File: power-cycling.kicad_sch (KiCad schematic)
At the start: 0 parts

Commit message: Updated sch power cycling section
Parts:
- added C?: C_100n_0402, antmicro-footprints:C_0402_1005Metric, symbol antmicroCapacitors0402:C_100n_0402
- added D? (x8): BZT52B15SV-T, antmicro-footprints:SOD-323, symbol antmicroDiodesZenerSingle:BZT52B15SV-T
- added Q? (x8): 2N7002K-T1-E3, antmicro-footprints:SOT-23-3, symbol antmicroTransistorsFETsMOSFETsSingle:2N7002K-T1-E3
- added QA? (x8), QB? (x8): SI7613DN-T1-GE3, antmicro-footprints:Vishay_PowerPAK_1212-8_Single, symbol antmicroTransistorsFETsMOSFETsSingle:SI7613DN-T1-GE3
- added R? (x6): R_0R_0402, antmicro-footprints:R_0402_1005Metric, symbol antmicroResistors0402:R_0R_0402
- added R? (x16): R_10k_0402, antmicro-footprints:R_0402_1005Metric, symbol antmicroResistors0402:R_10k_0402
- added R? (x16): R_2R_0402, antmicro-footprints:0402-res, symbol antmicroResistors0402:R_2R_0402
- added R? (x9): R_4k7_0402, antmicro-footprints:R_0402_1005Metric, symbol antmicroResistors0402:R_4k7_0402
- added TP? (x8): TP_1mm_SMD, antmicro-footprints:TP_SMD_1mm, symbol antmicroTestPoints:TP_1mm_SMD
- added U?: TCA9534, gpu-cluster-backplane-footprints:TSSOP-16, symbol gpu-cluster-backplane:TCA9534
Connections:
- new net: R?.1, R?.2, U?.3 (A2)
- new net: R?.1, R?.2, U?.1 (A0)
- new net: R?.2, U?.13 (~{INT})
- new net: R?.1, R?.2, U?.2 (A1)
- new net: QA?.4 (G), R?.2 (x8)
- new net: D?.A, Q?.3 (D), R?.1, R?.1, R?.2 (x8)
- new net: QB?.4 (G), R?.2 (x8)
- new net C_MEAS_1: QA?.5 (D), QB?.5 (D)
- new net C_MEAS_2: QA?.5 (D), QB?.5 (D)
- new net C_MEAS_3: QA?.5 (D), QB?.5 (D)
- new net C_MEAS_4: QA?.5 (D), QB?.5 (D)
- new net C_MEAS_5: QA?.5 (D), QB?.5 (D)
- new net C_MEAS_6: QA?.5 (D), QB?.5 (D)
- new net C_MEAS_7: QA?.5 (D), QB?.5 (D)
- new net C_MEAS_8: QA?.5 (D), QB?.5 (D)
- new net GND: C?.2, Q?.2 (S), Q?.2 (S), Q?.2 (S), Q?.2 (S), Q?.2 (S), Q?.2 (S), Q?.2 (S), Q?.2 (S), R?.2, R?.2, R?.2, R?.2, R?.2, R?.2, R?.2, R?.2, R?.2, R?.2, R?.2, U?.8 (GND)
- new net PC_1: Q?.1 (G), R?.1, R?.2, TP?.1, U?.4 (P0)
- new net PC_2: Q?.1 (G), R?.1, R?.2, TP?.1, U?.5 (P1)
- new net PC_3: Q?.1 (G), R?.1, R?.2, TP?.1, U?.6 (P2)
- new net PC_4: Q?.1 (G), R?.1, R?.2, TP?.1, U?.7 (P3)
- new net PC_5: Q?.1 (G), R?.1, R?.2, TP?.1, U?.9 (P4)
- new net PC_6: Q?.1 (G), R?.1, R?.2, TP?.1, U?.10 (P5)
- new net PC_7: Q?.1 (G), R?.1, R?.2, TP?.1, U?.11 (P6)
- new net PC_8: Q?.1 (G), R?.1, R?.2, TP?.1, U?.12 (P7)
- new net SCL: U?.14 (SCL)
- new net SDA: U?.15 (SDA)
- new net VCC12V0: D?.K, D?.K, D?.K, D?.K, D?.K, D?.K, D?.K, D?.K, QA?.1 (S), QA?.1 (S), QA?.1 (S), QA?.1 (S), QA?.1 (S), QA?.1 (S), QA?.1 (S), QA?.1 (S), QA?.2 (S), QA?.2 (S), QA?.2 (S), QA?.2 (S), QA?.2 (S), QA?.2 (S), QA?.2 (S), QA?.2 (S), QA?.3 (S), QA?.3 (S), QA?.3 (S), QA?.3 (S), QA?.3 (S), QA?.3 (S), QA?.3 (S), QA?.3 (S), QB?.1 (S), QB?.1 (S), QB?.1 (S), QB?.1 (S), QB?.1 (S), QB?.1 (S), QB?.1 (S), QB?.1 (S), QB?.2 (S), QB?.2 (S), QB?.2 (S), QB?.2 (S), QB?.2 (S), QB?.2 (S), QB?.2 (S), QB?.2 (S), QB?.3 (S), QB?.3 (S), QB?.3 (S), QB?.3 (S), QB?.3 (S), QB?.3 (S), QB?.3 (S), QB?.3 (S), R?.1, R?.1, R?.1, R?.1, R?.1, R?.1, R?.1, R?.1
- new net VCC3V3: C?.1, R?.1, R?.1, R?.1, R?.1, R?.1, R?.1, R?.1, R?.1, R?.1, R?.1, R?.1, R?.1, U?.16 (VDD)
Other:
- note added: "Arbiter for powering channels"
- note added: "GPIO EXPANDER for power cycling"
- note added: "I2C adress: 0x20"
- note added: "Key transistors' polarization TPs"
- note added: "Power Cycling"
- note added: "Power switching transistors"
- note added: "Remarks: Power can be switched on when: - signals from GPIO expander is enabled (pulled low) - GPU card module is inserted into slot"
- note added: "UP TO 15A"

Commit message: WIP Standarization
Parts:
- removed R? (x6): R_0R_0402, antmicro-footprints:R_0402_1005Metric, symbol antmicroResistors0402:R_0R_0402
- removed R?: R_4k7_0402, antmicro-footprints:R_0402_1005Metric, symbol antmicroResistors0402:R_4k7_0402
- removed U?: TCA9534, gpu-cluster-backplane-footprints:TSSOP-16, symbol gpu-cluster-backplane:TCA9534
- added R? (x6): R_0R_0402, antmicro-footprints:R_0402_1005Metric, symbol antmicroResistors0402:R_0R_0402
- added R?: R_4k7_0402, antmicro-footprints:R_0402_1005Metric, symbol antmicroResistors0402:R_4k7_0402
- added U?: TCA9534PWR, antmicro-footprints:TSSOP-16_4.4x5mm_P0.65mm, symbol antmicroInterfaceIOExpanders:TCA9534PWR
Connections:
- net GND: now also R?.2, R?.2, R?.2, U?.8 (GND)
- net PC_1: now also U?.4 (P0)
- net PC_2: now also U?.5 (P1)
- net PC_3: now also U?.6 (P2)
- net PC_4: now also U?.7 (P3)
- net PC_5: now also U?.9 (P4)
- net PC_6: now also U?.10 (P5)
- net PC_7: now also U?.11 (P6)
- net PC_8: now also U?.12 (P7)
- net SCL: now also U?.14 (SCL)
- net SDA: now also U?.15 (SDA)
- net VCC3V3: now also R?.1, R?.1, R?.1, R?.1, U?.16 (VDD)
- new net: R?.1, R?.2, U?.1 (A0)
- new net: R?.2, U?.13 (~{INT})
- new net: R?.1, R?.2, U?.2 (A1)
- new net: R?.1, R?.2, U?.3 (A2)
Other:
- moved on the sheet: C?

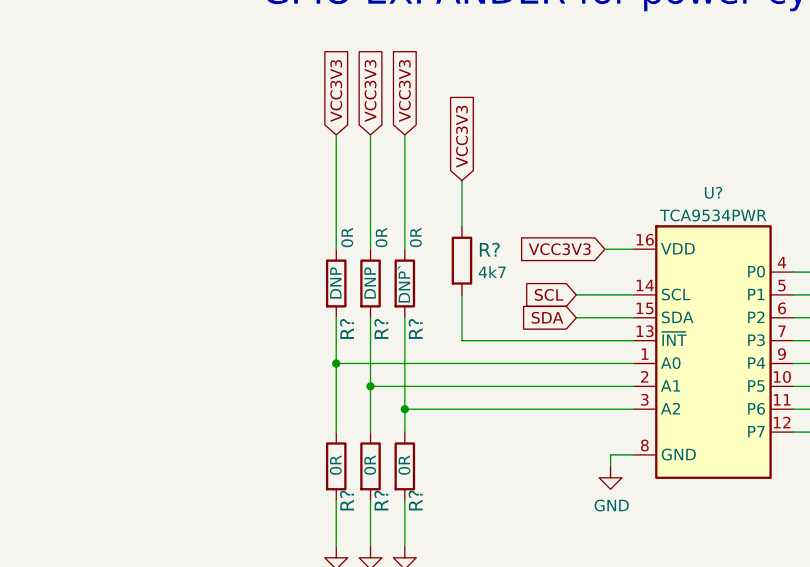
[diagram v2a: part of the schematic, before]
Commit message: Added debug section to schematic
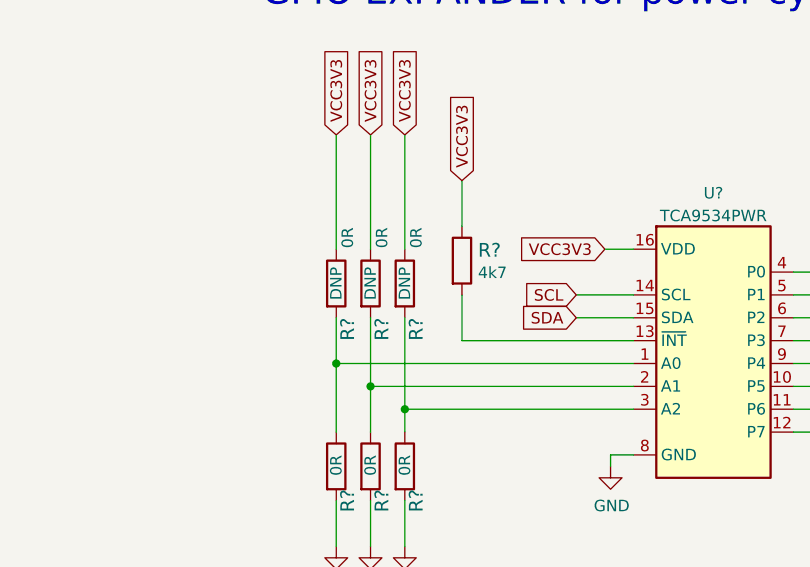
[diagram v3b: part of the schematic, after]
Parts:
- R?: DNP DNP` -> DNP
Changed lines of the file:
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@@
     )
     (property "Val" "0R" (id 6) (at 333.375 184.785 0))
-    (property "DNP" "DNP`" (id 7) (at 332.105 189.865 0))
+    (property "DNP" "DNP" (id 7) (at 332.105 189.865 0))
     (pin "1")
     (pin "2")

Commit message: Added function for enabling power after insertion of the card
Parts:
- added R? (x16): R_0R_0402, antmicro-footprints:R_0402_1005Metric, symbol antmicroResistors0402:R_0R_0402
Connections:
- net GND: now also R?.1, R?.1, R?.1, R?.1, R?.1, R?.1, R?.1, R?.1; no longer Q?.2 (S), Q?.2 (S), Q?.2 (S), Q?.2 (S), Q?.2 (S), Q?.2 (S), Q?.2 (S), Q?.2 (S)
- new net: Q?.2 (S), R?.1, R?.2 (x8)
- new net CARD_PRESENT_1: R?.2
- new net CARD_PRESENT_2: R?.2
- new net CARD_PRESENT_3: R?.2
- new net CARD_PRESENT_4: R?.2
- new net CARD_PRESENT_5: R?.2
- new net CARD_PRESENT_6: R?.2
- new net CARD_PRESENT_7: R?.2
- new net CARD_PRESENT_8: R?.2
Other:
- note added: "Remarks: Power can be switched on when: - signal from GPIO expander is not pulled low (pulled high by resistor) - GPU card module is inserted into slot (pulled low - connected to GND)"
- note removed: "Arbiter for powering channels"
- note removed: "Remarks: Power can be switched on when: - signals from GPIO expander is enabled (pulled low) - GPU card module is inserted into slot"
- moved on the sheet: C?, D?, Q?, QA?, QB?, R?, TP?, U?
